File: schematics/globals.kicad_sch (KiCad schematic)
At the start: 36 parts, among them J1 Power, Q6 2N7000, Q7 2N7000, U1 74HCU04, U2 74HC14, U3 ATF22V10C-7, U4 74HC590, U5 74HC590, U6 74HC590, U7 PicoROM32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

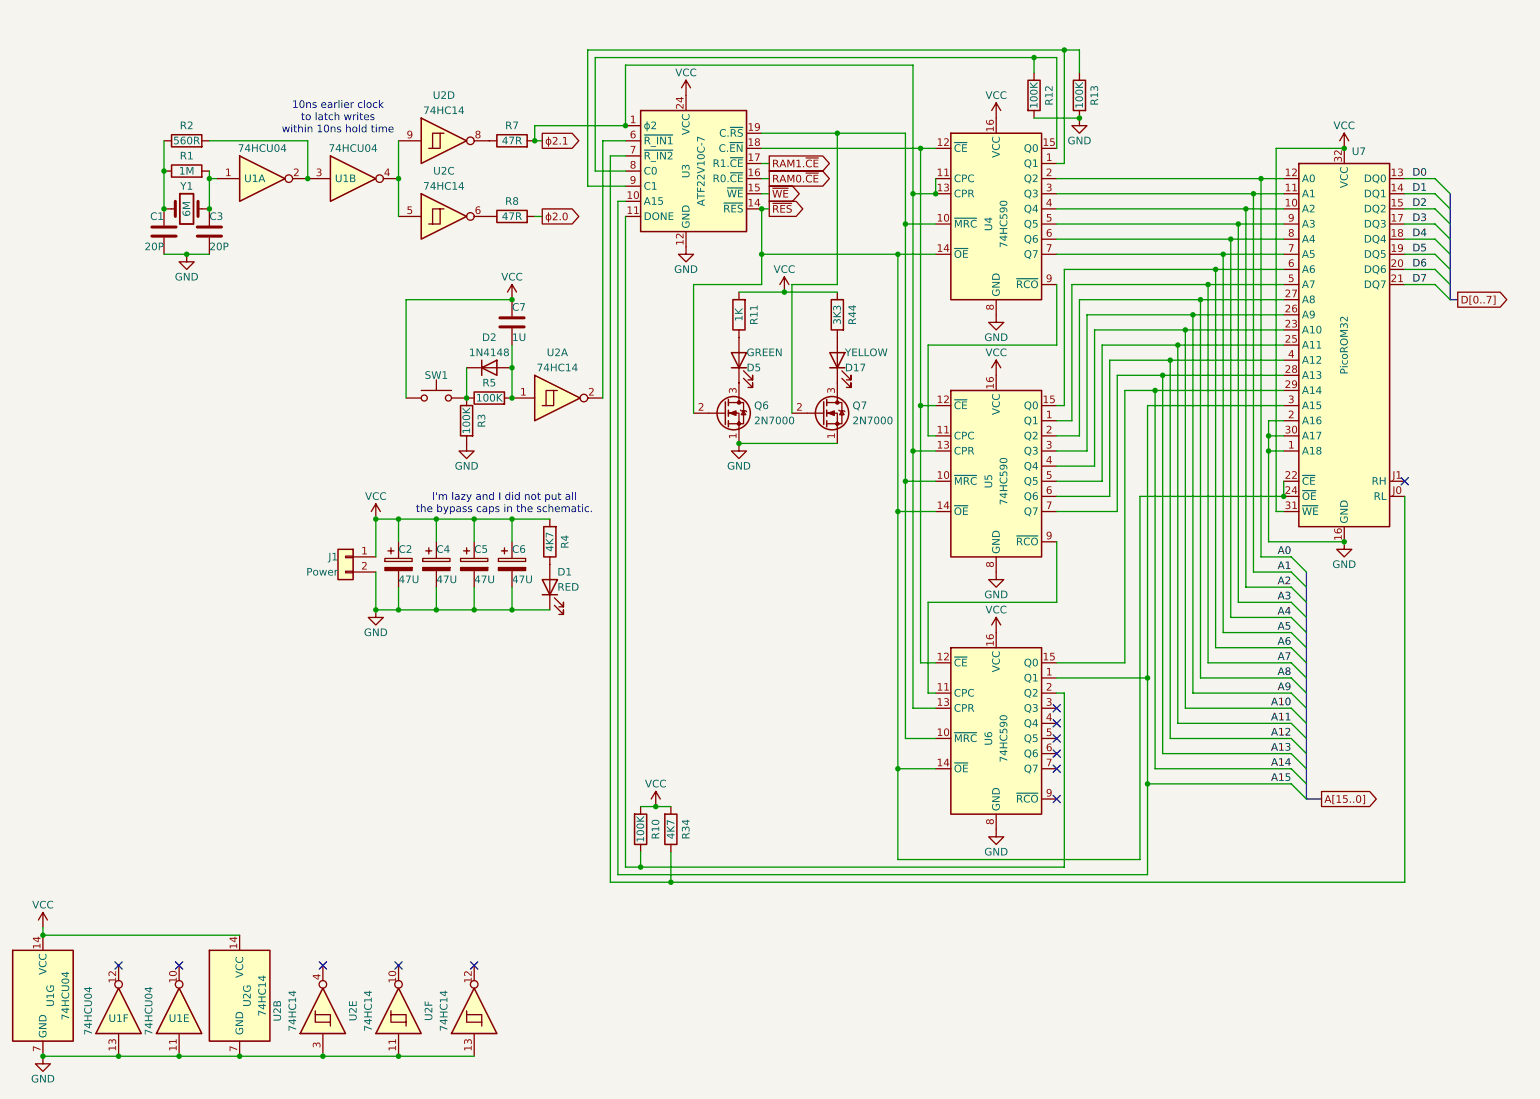
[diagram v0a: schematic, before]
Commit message: keyboard input works
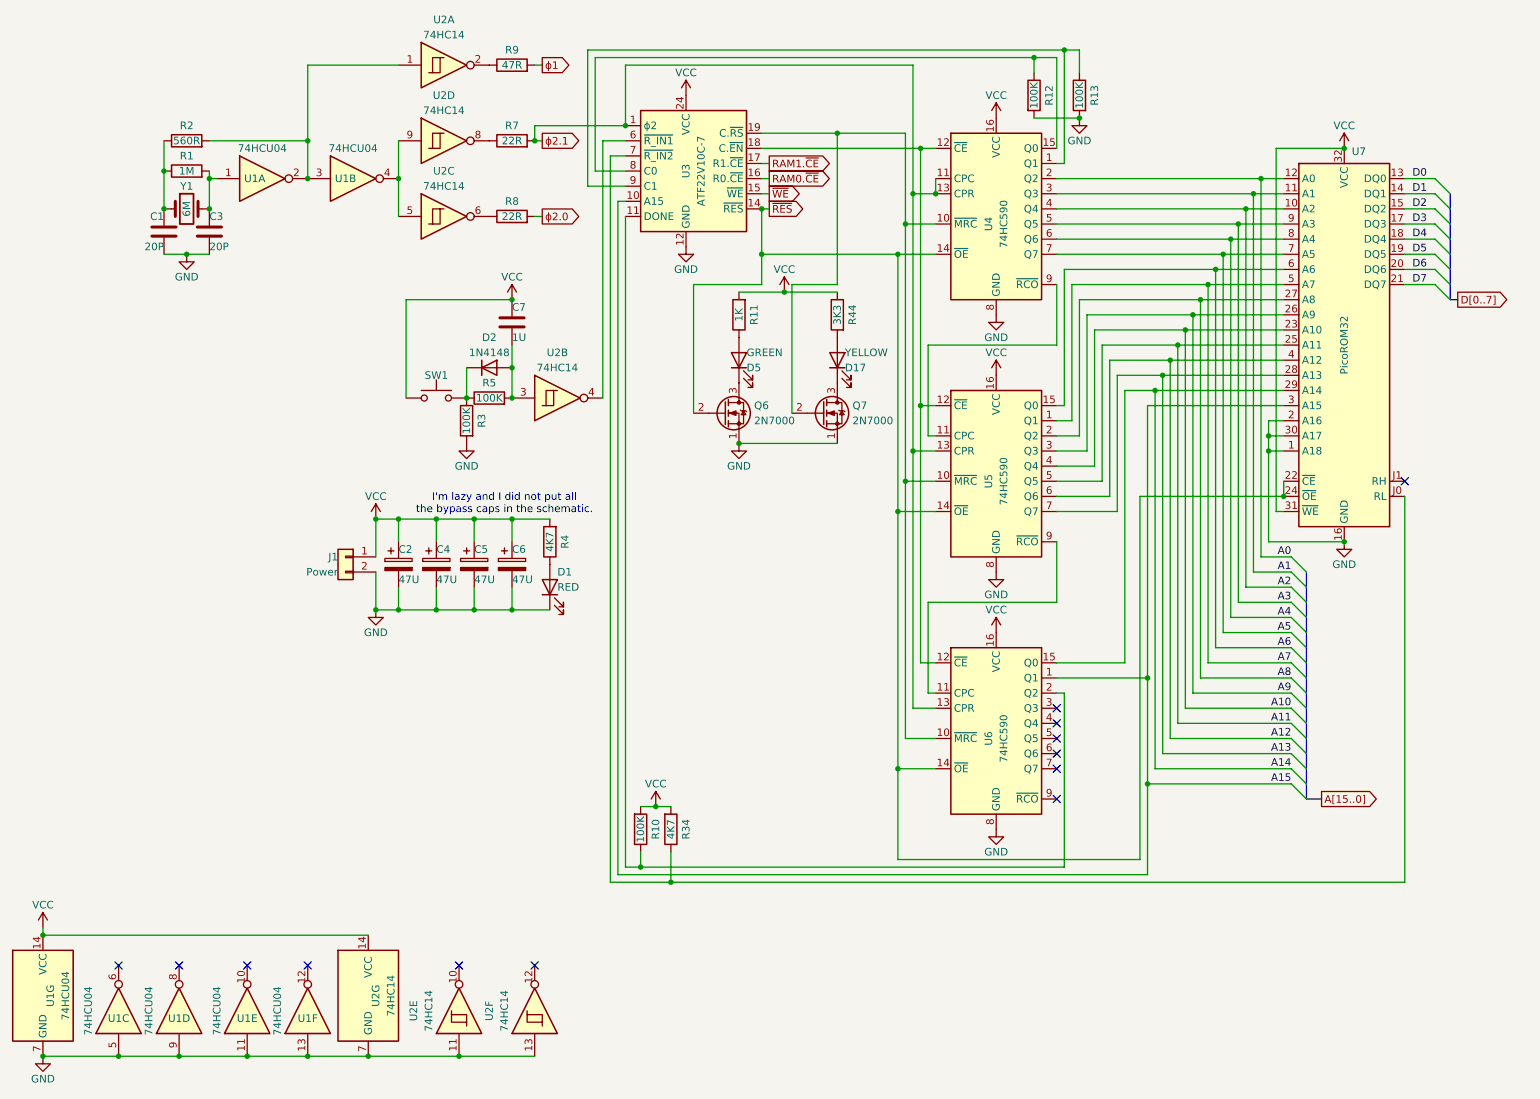
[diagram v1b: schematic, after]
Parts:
- added R9: 47R, symbol Device:R
- added unit 6 of U1
- added unit 5 of U1
- R7, R8: value 47R -> 22R
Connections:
- net GND: now also U1.5, U1.9, U1.11, U1.13; no longer U1.11, U1.13, U2.3
- net at C7.1, D2.2 (A), R5.2: now also U2.3; no longer U2.1
- net at R2.2, U1.2, U1.3: now also U2.1
- net at U3.6 (~{R_IN1}): now also U2.4; no longer U2.2
- new net: R9.1, U2.2
- new net ϕ1: R9.2
- no-connect marks 12 -> 13
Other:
- note removed: "10ns earlier clock to latch writes within 10ns hold time"
- moved on the sheet: U2A, U2E, U2F, U2G
